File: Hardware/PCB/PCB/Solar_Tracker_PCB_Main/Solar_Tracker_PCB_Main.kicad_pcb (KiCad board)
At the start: 4 copper layers, 94 x 96.5 mm, 65 parts, among them IC1 ESP32-S3-WROOM-1-N4R8, IC2 TPS54302DDCT, IC3 BNO085, IC4 PCF2131TFY, IC6 TLV76133DCYR, J1 SM08B-SRSS-TB_LF__SN_, J2 USB4940-00-A, J4 1977223-1, J5 1977223-1, J7 TB002-500-02BE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

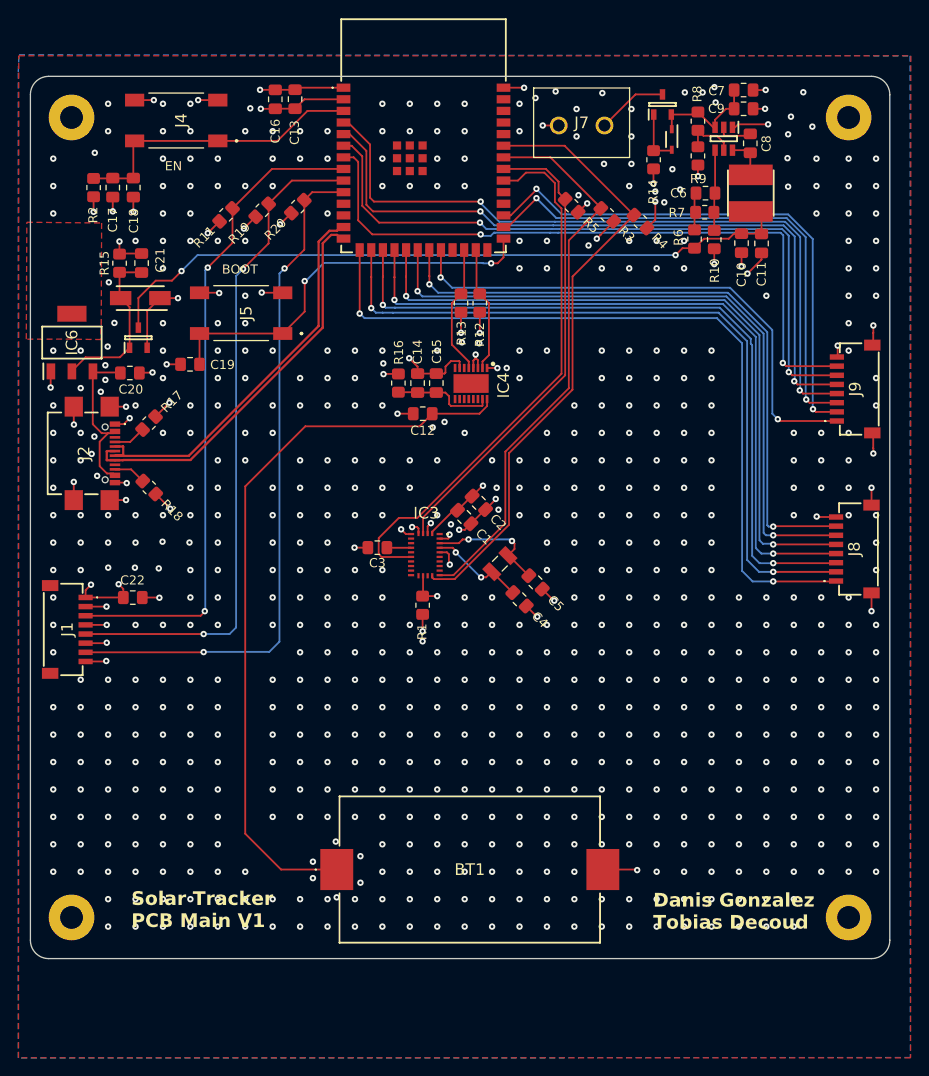
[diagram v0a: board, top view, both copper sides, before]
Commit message: Cambios, disminuir vias, pads en vdd
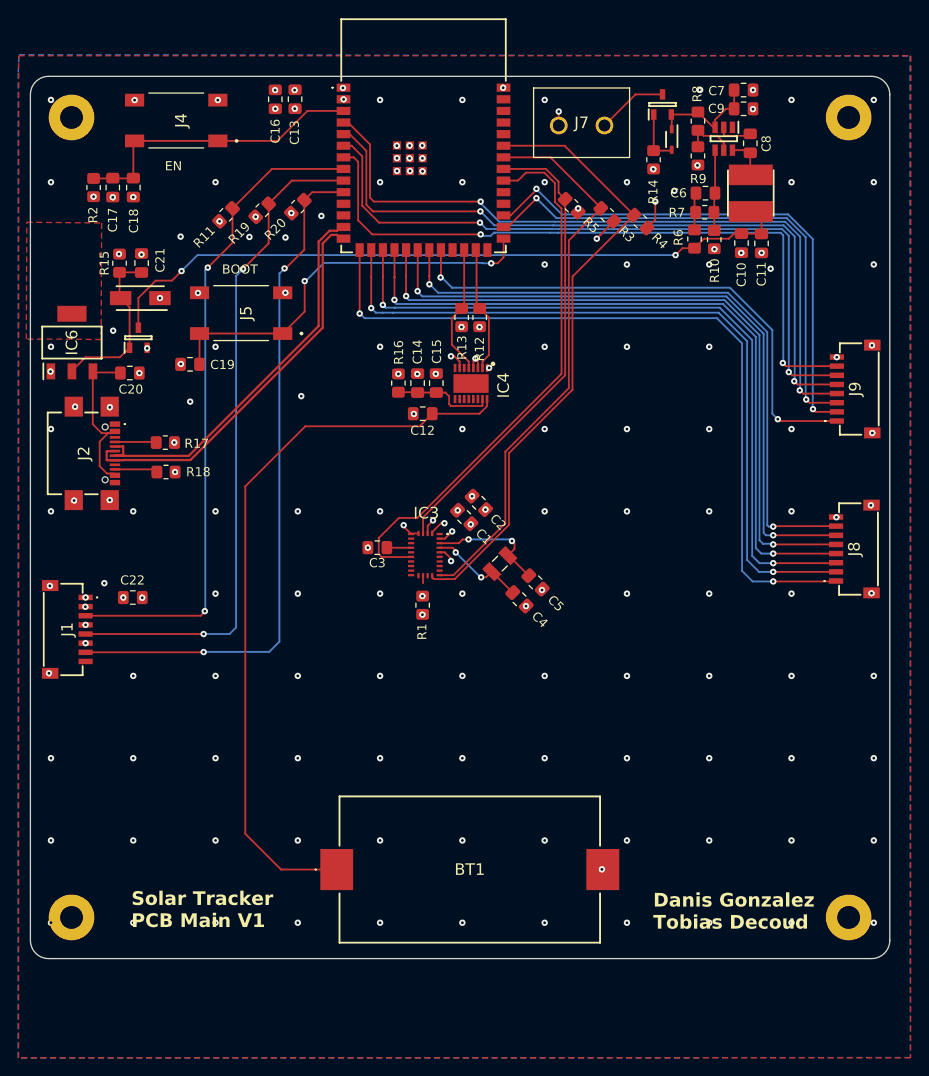
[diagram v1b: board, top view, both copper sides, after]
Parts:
- moved R17 2.78 mm to (86.3, 84.6), turned to 180 degrees
- moved R18 2.49 mm to (86.3, 87.8), turned to 0 degrees
- moved R13 1.58 mm to (118.7, 70.9)
- moved R12 1.58 mm to (120.6, 70.9)
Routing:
- net GND: track 126.7 -> 12.6 mm, vias 710 -> 165
- net VDD: track 56.7 -> 9.80 mm, vias 20 -> 23
- net Net-(J2-CC2): track 3.57 -> 4.70 mm
- net Net-(J2-CC1): track 3.58 -> 4.54 mm

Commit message: Agregue pines vdd y gnd
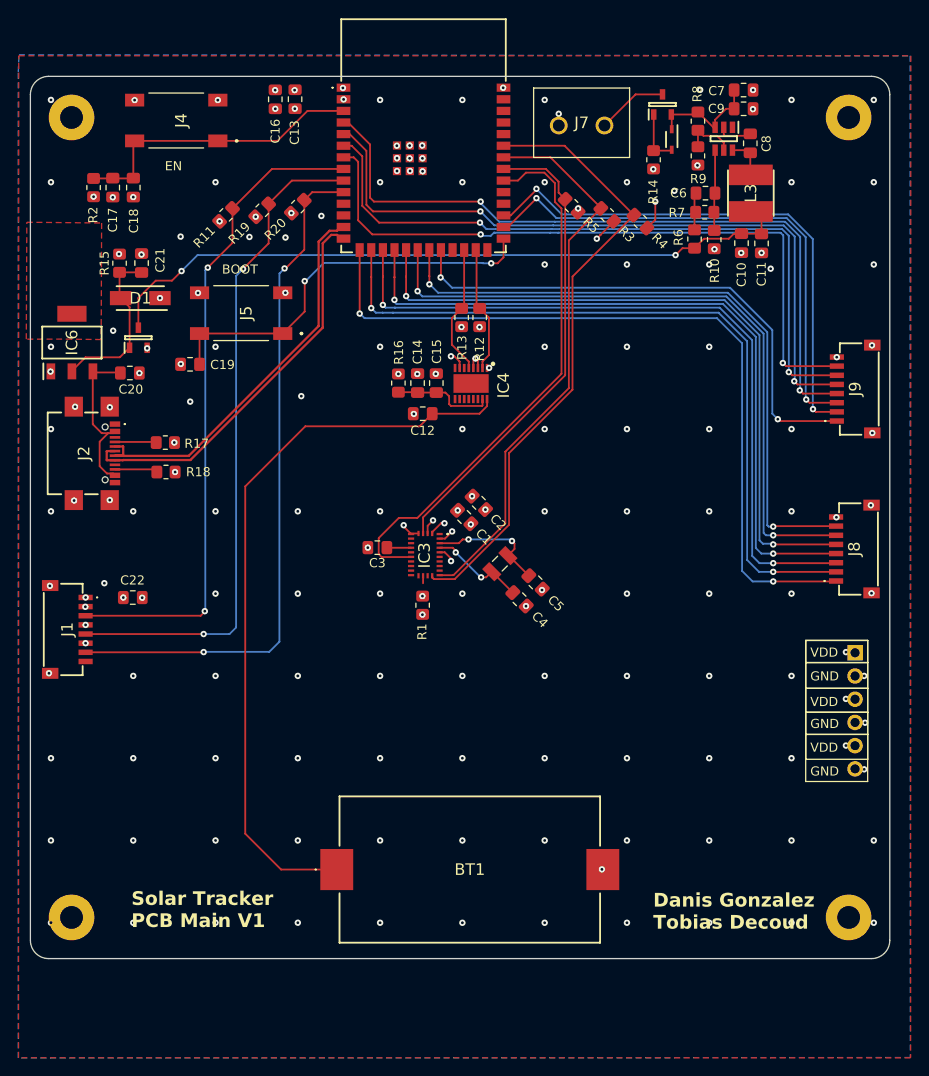
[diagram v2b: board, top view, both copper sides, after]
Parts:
- added J3: Conn_01x06_Pin, Connector_PinHeader_2.54mm:PinHeader_1x06_P2.54mm_Vertical, F.Cu at (161.7, 107.5)
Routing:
- net VDD: track 9.80 -> 11.8 mm, vias 23 -> 26
- net GND: track 12.6 -> 12.3 mm, vias 165 -> 166
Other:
- board text added: "GND"
- board text added: "VDD"

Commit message: actualizacion pcb
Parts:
- moved C5 1.76 mm to (126.9, 98.1), turned to 45 degrees
- moved C4 1.71 mm to (123.3, 101.5), turned to -135 degrees
- moved C22 1.50 mm to (81.2, 101.5)
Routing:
- net VDD: track 11.8 -> 13.5 mm, vias 26 -> 25
- net GND: track 12.3 -> 11.8 mm, vias 166 -> 167
- net /IMU/X_OUT: vias 2 -> 3
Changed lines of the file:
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@@
 	(footprint "Capacitor_SMD:C_0805_2012Metric_Pad1.18x1.45mm_HandSolder"
 		(layer "F.Cu")
-		(at 126.75 99.85 -45)
+		(at 126.9 98.1 45)
 		(descr "Capacitor SMD 0805 (2012 Metric), square (rectangular) end terminal, IPC-7351 nominal with elongated pad for handsoldering. (Body size source: IPC-SM-782 page 76, https://www.pcb-3d.com/wordpress/wp-content/uploads/ipc-sm-782a_amendment_1_and_2.pdf, https://docs.google.com/spreadsheets/d/1BsfQQcO9C6DZCsRaXUlFlo91Tg2WpOkGARC1WS5S8t0/edit?usp=sharing), generated with kicad-footprint-generator")
 		(tags "capacitor handsolder")
 		(property "Reference" "C5"
-			(at 3.2 0.05 135)
+			(at 3.2 0.05 45)
 			(layer "F.SilkS")
 			(effects
@@
 		)
 		(property "Value" "22p"
-			(at 0 1.679999 135)
+			(at 0 1.679999 45)
 			(layer "F.Fab")
 			(hide yes)
@@
 		)
 		(property "Datasheet" "~"
-			(at 0 0 135)
+			(at 0 0 45)
 			(layer "F.Fab")
 			(hide yes)
@@
 		)
 		(property "Description" "Polarized capacitor, small US symbol"
-			(at 0 0 135)
+			(at 0 0 45)
 			(layer "F.Fab")
 			(hide yes)
@@
 		(attr smd)
 		(fp_line
-			(start -0.261253 0.735)
-			(end 0.261253 0.735)
+			(start -0.261253 -0.735)
+			(end 0.261253 -0.735)
 			(stroke
 				(width 0.12)
@@
 		)
 		(fp_line
-			(start -0.261253 -0.735)
-			(end 0.261253 -0.735)
+			(start -0.261253 0.735)
+			(end 0.261253 0.735)
 			(stroke
 				(width 0.12)
@@
 		)
 		(pad "1" smd roundrect
-			(at -1.0375 0 315)
+			(at -1.0375 0 45)
 			(size 1.175 1.45)
 			(layers "F.Cu" "F.Mask" "F.Paste")
@@
 		)
 		(pad "2" smd roundrect
-			(at 1.0375 0 315)
+			(at 1.0375 0 45)
 			(size 1.175 1.45)
 			(layers "F.Cu" "F.Mask" "F.Paste")
@@
 	(footprint "Capacitor_SMD:C_0805_2012Metric_Pad1.18x1.45mm_HandSolder"
 		(layer "F.Cu")
-		(at 125 101.7 -45)
+		(at 123.3 101.5 -135)
 		(descr "Capacitor SMD 0805 (2012 Metric), square (rectangular) end terminal, IPC-7351 nominal with elongated pad for handsoldering. (Body size source: IPC-SM-782 page 76, https://www.pcb-3d.com/wordpress/wp-content/uploads/ipc-sm-782a_amendment_1_and_2.pdf, https://docs.google.com/spreadsheets/d/1BsfQQcO9C6DZCsRaXUlFlo91Tg2WpOkGARC1WS5S8t0/edit?usp=sharing), generated with kicad-footprint-generator")
 		(tags "capacitor handsolder")
 		(property "Reference" "C4"
-			(at 3.149999 0 135)
+			(at 3.149999 0 45)
 			(layer "F.SilkS")
 			(effects
@@
 		)
 		(property "Value" "22p"
-			(at 0 1.679999 135)
+			(at 0 1.679999 45)
 			(layer "F.Fab")
 			(hide yes)
@@
 		)
 		(property "Datasheet" "~"
-			(at 0 0 135)
+			(at 0 0 45)
 			(layer "F.Fab")
 			(hide yes)
@@
 		)
 		(property "Description" "Polarized capacitor, small US symbol"
-			(at 0 0 135)
+			(at 0 0 45)
 			(layer "F.Fab")
 			(hide yes)
@@
 		)
 		(pad "1" smd roundrect
-			(at -1.0375 0 315)
+			(at -1.0375 0 225)
 			(size 1.175 1.45)
 			(layers "F.Cu" "F.Mask" "F.Paste")
@@
 		)
 		(pad "2" smd roundrect
-			(at 1.0375 0 315)
+			(at 1.0375 0 225)
 			(size 1.175 1.45)
 			(layers "F.Cu" "F.Mask" "F.Paste")
@@
 	(footprint "Capacitor_SMD:C_0805_2012Metric_Pad1.18x1.45mm_HandSolder"
 		(layer "F.Cu")
-		(at 82.7 101.51)
+		(at 81.2 101.51)
 		(descr "Capacitor SMD 0805 (2012 Metric), square (rectangular) end terminal, IPC-7351 nominal with elongated pad for handsoldering. (Body size source: IPC-SM-782 page 76, https://www.pcb-3d.com/wordpress/wp-content/uploads/ipc-sm-782a_amendment_1_and_2.pdf, https://docs.google.com/spreadsheets/d/1BsfQQcO9C6DZCsRaXUlFlo91Tg2WpOkGARC1WS5S8t0/edit?usp=sharing), generated with kicad-footprint-generator")
 		(tags "capacitor handsolder")
@@
 	)
 	(segment
-		(start 81.6525 101.5)
-		(end 81.6625 101.51)
+		(start 133.85 61.85)
+		(end 135.307107 60.392893)
 		(width 0.2)
 		(layer "F.Cu")
@@
 	)
 	(segment
-		(start 133.85 61.85)
-		(end 135.307107 60.392893)
+		(start 85.7 70.4)
+		(end 85.7 68.79)
 		(width 0.2)
 		(layer "F.Cu")
@@
 	)
 	(segment
+		(start 85.7 68.79)
+		(end 85.67 68.76)
+		(width 0.2)
+		(layer "F.Cu")
+		(net 3)
+	)
+	(segment
 		(start 116.847 95.063)
 		(end 117.63 94.28)
@@
 	)
 	(via
-		(at 85.67 68.76)
+		(at 85.7 70.4)
 		(size 0.7)
 		(drill 0.3)
@@
 	)
 	(via
-		(at 81.6625 101.51)
-		(size 0.7)
-		(drill 0.3)
-		(layers "F.Cu" "B.Cu")
-		(net 3)
-	)
-	(via
 		(at 111.75 77.05)
 		(size 0.7)
@@
 	)
 	(via
+		(at 125.71 102.45)
+		(size 0.7)
+		(drill 0.3)
+		(layers "F.Cu" "B.Cu")
+		(net 5)
+	)
+	(via
 		(at 120.8 99.3)
 		(size 0.7)
@@
 	)
 	(segment
-		(start 113.95 94.5)
-		(end 113.09 94.5)
+		(start 113.2 94)
+		(end 113.7 94.5)
+		(width 0.2)
+		(layer "F.Cu")
+		(net 69)
+	)
+	(segment
+		(start 113.7 94.5)
+		(end 113.95 94.5)
 		(width 0.2)
 		(layer "F.Cu")
@@
 	)
 	(segment
-		(start 119.95 75.38)
-		(end 119.95 76.4)
+		(start 113.2 94.5)
+		(end 113.137 94.563)
 		(width 0.2)
 		(layer "F.Cu")
@@
 	)
 	(segment
-		(start 112.33 93.74)
-		(end 112.33 93.6)
+		(start 119.95 75.38)
+		(end 119.95 76.4)
 		(width 0.2)
 		(layer "F.Cu")
@@
 	)
 	(segment
-		(start 117.5 75.12)
-		(end 117.872 75.12)
+		(start 113.2 94)
+		(end 113.2 94.5)
 		(width 0.2)
 		(layer "F.Cu")
@@
 	)
 	(segment
-		(start 113.09 94.5)
-		(end 112.33 93.74)
+		(start 117.5 75.12)
+		(end 117.872 75.12)
 		(width 0.2)
 		(layer "F.Cu")
@@
 	)
 	(via
-		(at 112.33 93.6)
+		(at 113.2 94)
 		(size 0.7)
 		(drill 0.3)
@@
 	)
 	(via
-		(at 89.83 68.19)
+		(at 88.4 68.19)
 		(size 0.7)
 		(drill 0.3)
@@
 	)
 	(via
+		(at 86.6 70.4)
+		(size 0.7)
+		(drill 0.3)
+		(layers "F.Cu" "B.Cu")
+		(net 69)
+	)
+	(via
 		(at 127.75 119.08)
 		(size 0.7)
@@
 	)
 	(via
-		(at 125.71 102.45)
+		(at 83.65 63.99)
 		(size 0.7)
 		(drill 0.3)
@@
 	)
 	(via
-		(at 83.65 63.99)
+		(at 109.75 101.08)
 		(size 0.7)
 		(drill 0.3)
@@
 	)
 	(via
-		(at 109.75 101.08)
+		(at 162.8 115.2)
 		(size 0.7)
 		(drill 0.3)
@@
 	)
 	(via
-		(at 162.8 115.2)
+		(at 127.75 83.08)
 		(size 0.7)
 		(drill 0.3)
@@
 	)
 	(via
-		(at 127.75 83.08)
+		(at 82.4 99.9)
 		(size 0.7)
 		(drill 0.3)

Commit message: cambios pcb main
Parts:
- moved C5 6.43 mm to (123.0, 93.0), turned to 90 degrees
- moved C4 4.65 mm to (123.0, 96.9), turned to 90 degrees
- moved Y1 3.06 mm to (120.0, 96.8), turned to -90 degrees
- moved C2 0.97 mm to (119.8, 90.5)
- moved C1 0.93 mm to (118.4, 91.9)
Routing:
- net GND: track 11.8 -> 90.1 mm, vias 167 -> 163
- net VDD: track 13.5 -> 45.5 mm, vias 25 -> 22
- net /IMU/X_IN: track 13.4 -> 7.36 mm, vias 2 -> 0
- net IMU_SCL: track 68.1 -> 71.9 mm
- net IMU_SDA: track 61.3 -> 65.1 mm
- net /IMU/X_OUT: track 10.6 -> 7.61 mm, vias 3 -> 0

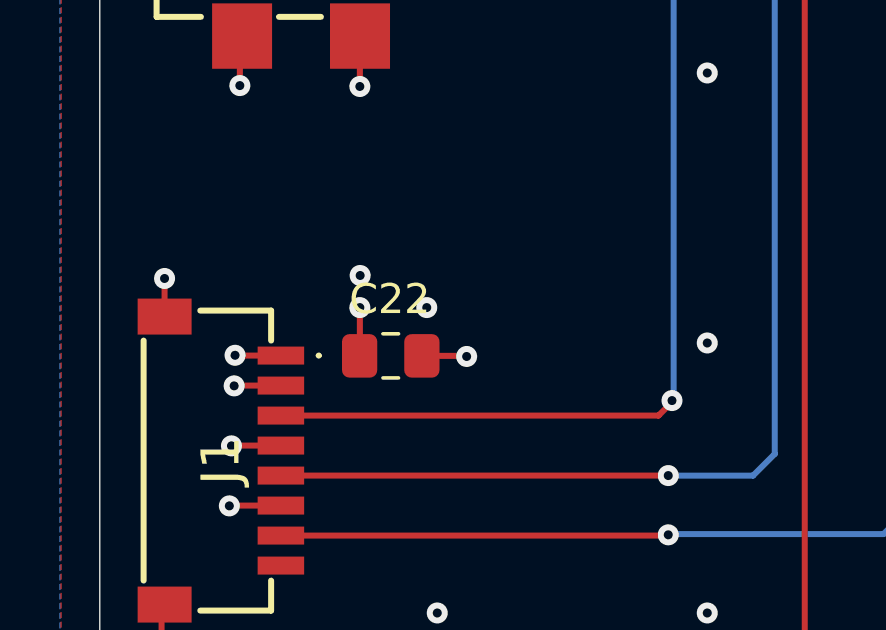
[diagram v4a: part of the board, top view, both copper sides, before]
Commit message: Actualizacion capactiores desacoplo hacia placa satelite
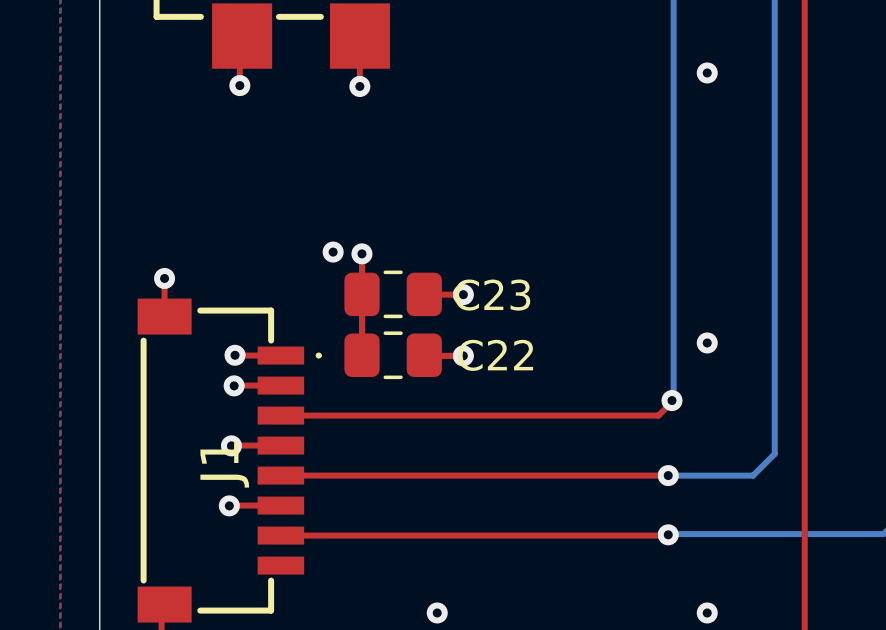
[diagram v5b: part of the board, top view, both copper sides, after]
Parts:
- added C23: 100n, Capacitor_SMD:C_0805_2012Metric_Pad1.18x1.45mm_HandSolder, F.Cu at (81.3, 99.5)
- moved C22 0.08 mm to (81.3, 101.5)
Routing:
- net VDD: track 45.5 -> 47.3 mm
- net GND: track 90.1 -> 91.2 mm
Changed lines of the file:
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@@
 	(footprint "Capacitor_SMD:C_0805_2012Metric_Pad1.18x1.45mm_HandSolder"
 		(layer "F.Cu")
+		(at 81.28 99.46)
+		(descr "Capacitor SMD 0805 (2012 Metric), square (rectangular) end terminal, IPC-7351 nominal with elongated pad for handsoldering. (Body size source: IPC-SM-782 page 76, https://www.pcb-3d.com/wordpress/wp-content/uploads/ipc-sm-782a_amendment_1_and_2.pdf, https://docs.google.com/spreadsheets/d/1BsfQQcO9C6DZCsRaXUlFlo91Tg2WpOkGARC1WS5S8t0/edit?usp=sharing), generated with kicad-footprint-generator")
+		(tags "capacitor handsolder")
+		(property "Reference" "C23"
+			(at 3.33 0.06 0)
+			(layer "F.SilkS")
+			(effects
+				(font
+					(size 1 1)
+					(thickness 0.15)
+				)
+			)
+		)
+		(property "Value" "100n"
+			(at 0 1.68 0)
+			(layer "F.Fab")
+			(hide yes)
+			(effects
+				(font
+					(size 1 1)
+					(thickness 0.15)
+				)
+			)
+		)
+		(property "Datasheet" "~"
+			(at 0 0 0)
+			(layer "F.Fab")
+			(hide yes)
+			(effects
+				(font
+					(size 1.27 1.27)
+					(thickness 0.15)
+				)
+			)
+		)
+		(property "Description" "Unpolarized capacitor"
+			(at 0 0 0)
+			(layer "F.Fab")
+			(hide yes)
+			(effects
+				(font
+					(size 1.27 1.27)
+					(thickness 0.15)
+				)
+			)
+		)
+		(property ki_fp_filters "C_*")
+		(sheetname "/MCU/")
+		(sheetfile "MCU.kicad_sch")
+		(attr smd)
+		(fp_line
+			(start -0.261252 -0.735)
+			(end 0.261252 -0.735)
+			(stroke
+				(width 0.12)
+				(type solid)
+			)
+			(layer "F.SilkS")
+		)
+		(fp_line
+			(start -0.261252 0.735)
+			(end 0.261252 0.735)
+			(stroke
+				(width 0.12)
+				(type solid)
+			)
+			(layer "F.SilkS")
+		)
+		(fp_rect
+			(start -1.88 -0.98)
+			(end 1.88 0.98)
+			(stroke
+				(width 0.05)
+				(type solid)
+			)
+			(fill no)
+			(layer "F.CrtYd")
+		)
+		(fp_rect
+			(start -1 -0.625)
+			(end 1 0.625)
+			(stroke
+				(width 0.1)
+				(type solid)
+			)
+			(fill no)
+			(layer "F.Fab")
+		)
+		(pad "1" smd roundrect
+			(at -1.0375 0)
+			(size 1.175 1.45)
+			(layers "F.Cu" "F.Mask" "F.Paste")
+			(roundrect_rratio 0.212766)
+			(net 3 "VDD")
+			(pintype "passive")
+		)
+		(pad "2" smd roundrect
+			(at 1.0375 0)
+			(size 1.175 1.45)
+			(layers "F.Cu" "F.Mask" "F.Paste")
+			(roundrect_rratio 0.212766)
+			(net 69 "GND")
+			(pintype "passive")
+		)
+		(embedded_fonts no)
+		(model "${KICAD9_3DMODEL_DIR}/Capacitor_SMD.3dshapes/C_0805_2012Metric.step"
+			(offset
+				(xyz 0 0 0)
+			)
+			(scale
+				(xyz 1 1 1)
+			)
+			(rotate
+				(xyz 0 0 0)
+			)
+		)
+	)
+	(footprint "Capacitor_SMD:C_0805_2012Metric_Pad1.18x1.45mm_HandSolder"
+		(layer "F.Cu")
 		(at 151.47 62.77625 90)
 		(descr "Capacitor SMD 0805 (2012 Metric), square (rectangular) end terminal, IPC-7351 nominal with elongated pad for handsoldering. (Body size source: IPC-SM-782 page 76, https://www.pcb-3d.com/wordpress/wp-content/uploads/ipc-sm-782a_amendment_1_and_2.pdf, https://docs.google.com/spreadsheets/d/1BsfQQcO9C6DZCsRaXUlFlo91Tg2WpOkGARC1WS5S8t0/edit?usp=sharing), generated with kicad-footprint-generator")
@@
 	(footprint "Capacitor_SMD:C_0805_2012Metric_Pad1.18x1.45mm_HandSolder"
 		(layer "F.Cu")
-		(at 81.2 101.51)
+		(at 81.28 101.49)
 		(descr "Capacitor SMD 0805 (2012 Metric), square (rectangular) end terminal, IPC-7351 nominal with elongated pad for handsoldering. (Body size source: IPC-SM-782 page 76, https://www.pcb-3d.com/wordpress/wp-content/uploads/ipc-sm-782a_amendment_1_and_2.pdf, https://docs.google.com/spreadsheets/d/1BsfQQcO9C6DZCsRaXUlFlo91Tg2WpOkGARC1WS5S8t0/edit?usp=sharing), generated with kicad-footprint-generator")
 		(tags "capacitor handsolder")
 		(property "Reference" "C22"
-			(at -0.03 -1.89 0)
+			(at 3.45 0.04 0)
 			(layer "F.SilkS")
 			(effects
@@
 	)
 	(segment
+		(start 80.2425 101.49)
+		(end 80.2425 99.46)
+		(width 0.2)
+		(layer "F.Cu")
+		(net 3)
+	)
+	(segment
 		(start 99.37 48.37)
 		(end 99.7025 48.0375)
@@
 	)
 	(segment
-		(start 80.17 99.9)
-		(end 80.17 101.5025)
-		(width 0.2)
-		(layer "F.Cu")
-		(net 3)
-	)
-	(segment
 		(start 120.02 91.777246)
 		(end 120.533623 91.263623)
@@
 	)
 	(segment
+		(start 80.2425 99.46)
+		(end 80.2425 98.1125)
+		(width 0.2)
+		(layer "F.Cu")
+		(net 3)
+	)
+	(segment
 		(start 132.369972 58.380028)
 		(end 131.407107 59.342893)
@@
 	)
 	(segment
+		(start 80.2425 98.1125)
+		(end 80.24 98.11)
+		(width 0.2)
+		(layer "F.Cu")
+		(net 3)
+	)
+	(segment
 		(start 131.407107 59.342893)
 		(end 131.407107 59.357107)
@@
 	)
 	(via
-		(at 80.17 99.9)
+		(at 80.24 98.11)
 		(size 0.7)
 		(drill 0.3)
@@
 	)
 	(segment
+		(start 83.62 101.51)
+		(end 82.2375 101.51)
+		(width 0.2)
+		(layer "F.Cu")
+		(net 69)
+	)
+	(segment
 		(start 86.6 75.97)
 		(end 87.895 75.97)
@@
 	)
 	(segment
-		(start 83.71 101.51)
-		(end 83.73 101.53)
-		(width 0.2)
-		(layer "F.Cu")
-		(net 69)
-	)
-	(segment
 		(start 118.45 75.698)
 		(end 118.45 76.4)
@@
 	)
 	(segment
-		(start 82.2375 101.51)
-		(end 83.71 101.51)
+		(start 120.45 75.46)
+		(end 120.45 76.4)
 		(width 0.2)
 		(layer "F.Cu")
@@
 	)
 	(segment
-		(start 120.45 75.46)
-		(end 120.45 76.4)
+		(start 83.62 99.47)
+		(end 82.3275 99.47)
 		(width 0.2)
 		(layer "F.Cu")
@@
 	)
 	(segment
+		(start 82.3275 99.47)
+		(end 82.3175 99.46)
+		(width 0.2)
+		(layer "F.Cu")
+		(net 69)
+	)
+	(segment
 		(start 76.17 92.5)
 		(end 76.17 90.9255)
@@
 	)
 	(via
-		(at 100.75 119.08)
+		(at 83.62 99.47)
 		(size 0.7)
 		(drill 0.3)
@@
 	)
 	(via
-		(at 118.75 137.08)
+		(at 100.75 119.08)
 		(size 0.7)
 		(drill 0.3)
@@
 	)
 	(via
-		(at 80.18 98.83)
+		(at 118.75 137.08)
 		(size 0.7)
 		(drill 0.3)
@@
 	)
 	(via
-		(at 83.73 101.53)
+		(at 83.62 101.51)
 		(size 0.7)
 		(drill 0.3)
@@
 	)
 	(via
+		(at 79.28 98.05)
+		(size 0.7)
+		(drill 0.3)
+		(layers "F.Cu" "B.Cu")
+		(net 69)
+	)
+	(via
 		(at 160.2 116.72)
 		(size 0.7)
@@
 		(size 0.7)
 		(drill 0.3)
-		(layers "F.Cu" "B.Cu")
-		(net 69)
-	)
-	(via
-		(at 82.4 99.9)
-		(size 0.7)
-		(drill 0.3)

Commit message: cambios main
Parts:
- moved Y1 0.26 mm to (119.7, 96.8)
- moved C4 0.19 mm to (122.8, 96.9)
- moved C5 0.19 mm to (122.8, 93.0)
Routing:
- net VDD: track 47.3 -> 50.0 mm
- net IMU_SDA: track 65.1 -> 66.9 mm
- net IMU_SCL: track 71.9 -> 73.6 mm
- net GND: track 91.2 -> 92.0 mm, vias 163 -> 173
